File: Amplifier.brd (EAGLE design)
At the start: 60.3 x 55.2 mm, 34 parts, among them IC1 OP213, J1 ARDUINO_R3_SHIELD

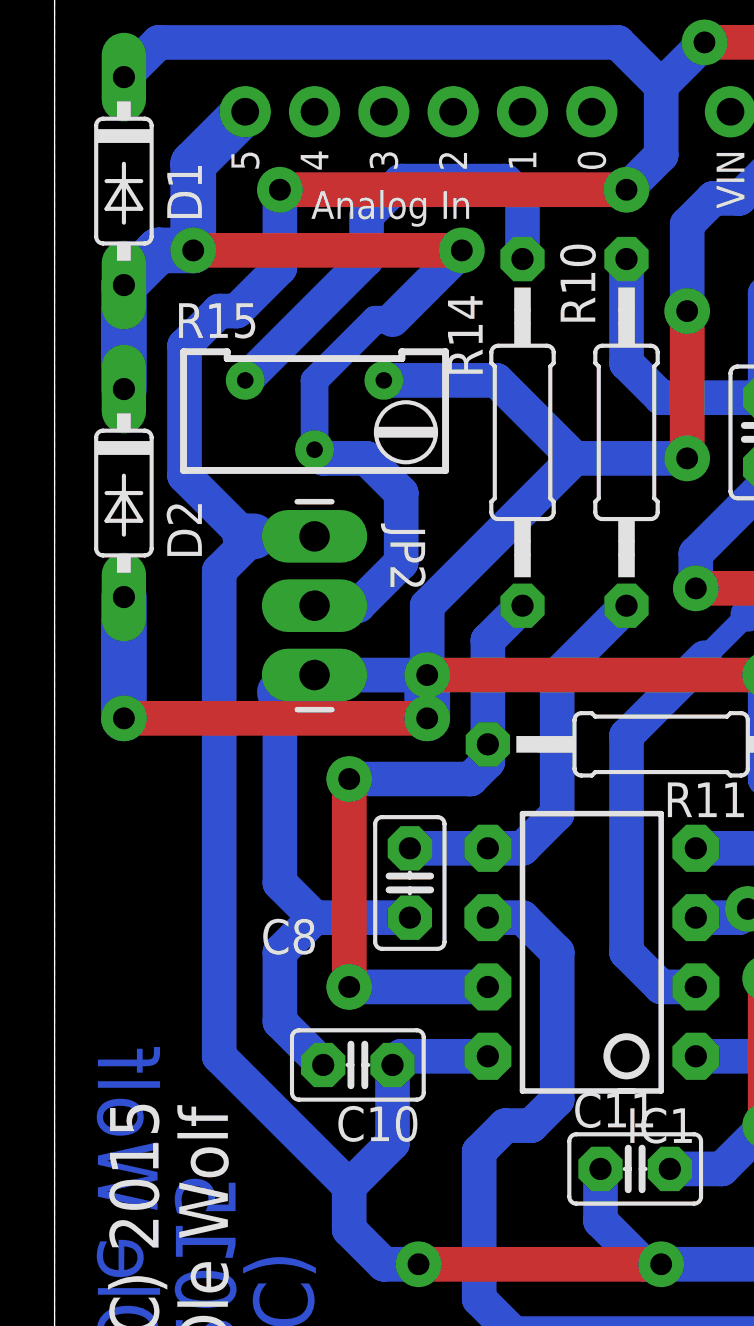
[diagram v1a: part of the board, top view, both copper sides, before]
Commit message: Bug in output stage fixed, redundant capacitor removed.
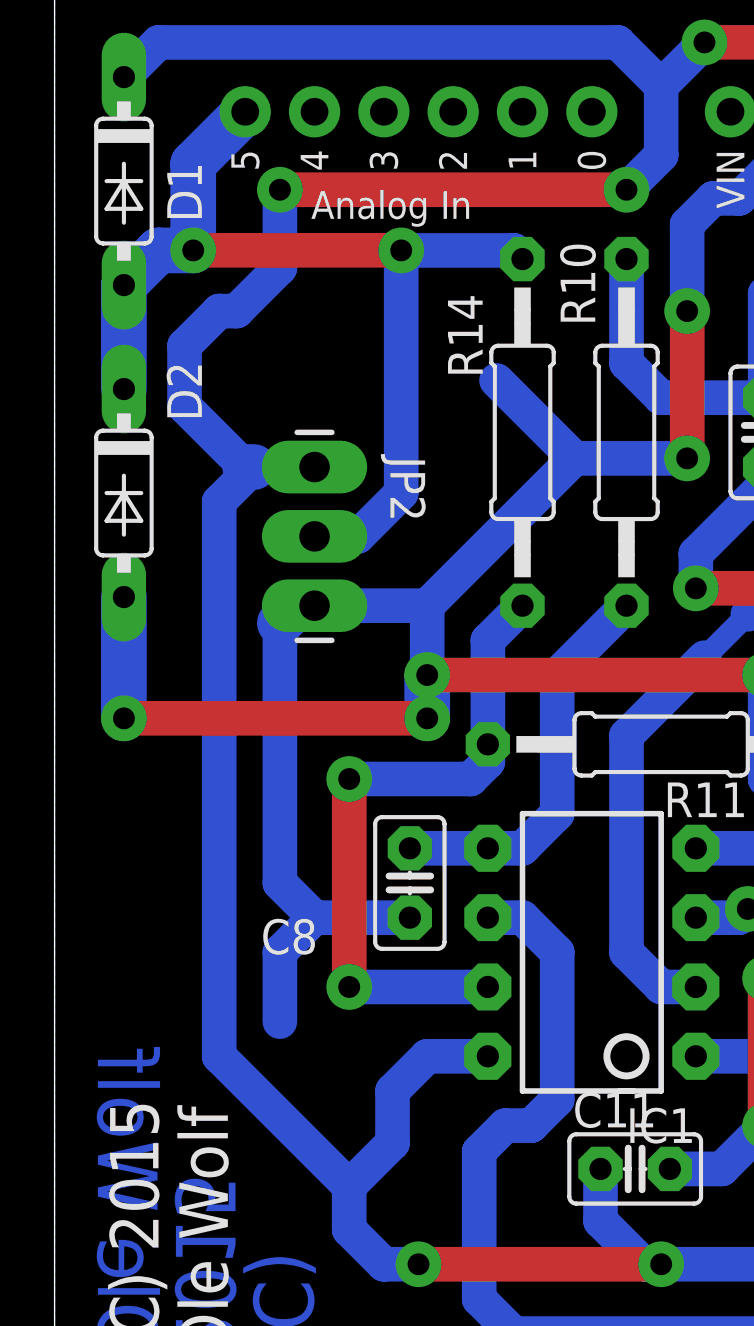
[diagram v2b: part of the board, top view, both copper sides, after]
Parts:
- removed C10: 100n, rcl:C025-025X050
- removed R15: 4k7, rcl:RTRIM64Y
- moved JP2 2.54 mm to (9.53, 32.7)
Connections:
- removed net N$18: R14.1, R15.3
- net GEOPHONE_OUT: now also R14.1; no longer R15.2
- net GND: no longer C10.2, R15.1
- net VCC: no longer C10.1
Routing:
- net N$18: track 16.6 -> 0.00 mm
- net GEOPHONE_OUT: track 42.7 -> 37.7 mm
- net GND: track 166.8 -> 163.0 mm
- net VCC: track 166.8 -> 166.3 mm
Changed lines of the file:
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@@
 <attribute name="VALUE" x="16.4592" y="41.3385" size="1.27" layer="27" ratio="10" rot="R270"/>
 </element>
-<element name="JP2" library="SparkFun-Connectors" package="1X03_LONGPADS" value="Out" x="9.525" y="30.1625" smashed="yes" rot="R90">
-<attribute name="NAME" x="12.3063" y="35.6362" size="1.27" layer="25" ratio="10" rot="SR270"/>
-<attribute name="VALUE" x="5.3975" y="33.02" size="1.27" layer="27" rot="SR270"/>
-</element>
-<element name="C10" library="rcl" package="C025-025X050" value="100n" x="11.1125" y="15.875" smashed="yes" rot="R180">
-<attribute name="NAME" x="13.3985" y="14.351" size="1.27" layer="25" ratio="10" rot="R180"/>
-<attribute name="VALUE" x="13.716" y="12.6365" size="1.27" layer="27" ratio="10" rot="R180"/>
-</element>
-<element name="R15" library="rcl" package="RTRIM64Y" value="4k7" x="9.525" y="40.9575" smashed="yes" rot="R90">
-<attribute name="NAME" x="7.49" y="43.785" size="1.27" layer="25" rot="R180"/>
-<attribute name="VALUE" x="11.6175" y="43.7075" size="1.27" layer="27" rot="R180"/>
+<element name="JP2" library="SparkFun-Connectors" package="1X03_LONGPADS" value="Out" x="9.525" y="32.7025" smashed="yes" rot="R90">
+<attribute name="NAME" x="12.3063" y="38.1762" size="1.27" layer="25" ratio="10" rot="SR270"/>
+<attribute name="VALUE" x="5.3975" y="36.83" size="1.27" layer="27" rot="SR270"/>
 </element>
 <element name="J1" library="SparkFun-Boards" package="UNO_R3_SHIELD" value="ARDUINO_R3_SHIELD" x="61.595" y="0" rot="R90"/>
@@
 </element>
 <element name="D2" library="diode" package="DO35-7" value="1N4148DO35-7" x="2.54" y="36.83" smashed="yes" rot="R270">
-<attribute name="NAME" x="4.1275" y="36.576" size="1.27" layer="25" ratio="10" rot="R270"/>
+<attribute name="NAME" x="4.1275" y="41.656" size="1.27" layer="25" ratio="10" rot="R270"/>
 </element>
 <element name="JP3" library="pinhead" package="1X03" value="" x="48.895" y="50.165" smashed="yes">
@@
 <contactref element="IC1" pad="8"/>
 <contactref element="JP2" pad="3"/>
-<contactref element="C10" pad="1"/>
-<wire x1="7.3025" y1="35.2425" x2="6.0325" y2="33.9725" width="1.27" layer="16"/>
-<wire x1="6.0325" y1="33.9725" x2="6.0325" y2="16.1925" width="1.27" layer="16"/>
-<wire x1="15.875" y1="16.1925" x2="12.7" y2="16.1925" width="1.27" layer="16"/>
-<wire x1="12.7" y1="16.1925" x2="12.3825" y2="15.875" width="1.27" layer="16"/>
+<wire x1="7.3025" y1="37.7825" x2="6.0325" y2="36.5125" width="1.27" layer="16"/>
+<wire x1="6.0325" y1="36.5125" x2="6.0325" y2="16.1925" width="1.27" layer="16"/>
 <wire x1="40.005" y1="6.0325" x2="40.005" y2="7.3025" width="1.27" layer="16"/>
 <wire x1="40.005" y1="7.3025" x2="38.735" y2="8.5725" width="1.27" layer="16"/>
@@
 <wire x1="22.225" y1="8.5725" x2="13.335" y2="8.5725" width="1.27" layer="1"/>
 <via x="13.335" y="8.5725" extent="1-16" drill="0.8" diameter="1.6764" shape="square"/>
-<wire x1="7.3025" y1="35.2425" x2="6.985" y2="35.2425" width="1.6764" layer="16"/>
-<wire x1="6.985" y1="35.2425" x2="4.7625" y2="37.465" width="1.27" layer="16"/>
-<wire x1="4.7625" y1="37.465" x2="4.7625" y2="42.2275" width="1.27" layer="16"/>
+<wire x1="7.3025" y1="37.7825" x2="6.985" y2="37.7825" width="1.6764" layer="16"/>
+<wire x1="6.985" y1="37.7825" x2="4.7625" y2="40.005" width="1.27" layer="16"/>
+<wire x1="4.7625" y1="40.005" x2="4.7625" y2="42.2275" width="1.27" layer="16"/>
 <wire x1="4.7625" y1="42.2275" x2="6.0325" y2="43.4975" width="1.27" layer="16"/>
 <wire x1="6.0325" y1="43.4975" x2="6.6675" y2="43.4975" width="1.27" layer="16"/>
@@
 <wire x1="8.255" y1="45.085" x2="8.255" y2="47.9425" width="1.27" layer="16"/>
 <via x="8.255" y="47.9425" extent="1-16" drill="0.8" diameter="1.6764" shape="square"/>
-<wire x1="9.525" y1="35.2425" x2="7.3025" y2="35.2425" width="1.27" layer="16"/>
+<wire x1="9.525" y1="37.7825" x2="7.3025" y2="37.7825" width="1.27" layer="16"/>
 <wire x1="8.255" y1="47.9425" x2="20.955" y2="47.9425" width="1.27" layer="1"/>
 <via x="20.955" y="47.9425" extent="1-16" drill="0.8" diameter="1.6764" shape="square"/>
@@
 <wire x1="10.795" y1="9.8425" x2="12.065" y2="8.5725" width="1.27" layer="16"/>
 <wire x1="12.065" y1="8.5725" x2="13.335" y2="8.5725" width="1.27" layer="16"/>
-<wire x1="12.3825" y1="15.875" x2="12.3825" y2="13.0175" width="1.27" layer="16"/>
 <wire x1="12.3825" y1="13.0175" x2="10.795" y2="11.43" width="1.27" layer="16"/>
 <contactref element="C11" pad="1"/>
@@
 <wire x1="53.6575" y1="50.8" x2="54.9275" y2="49.53" width="1.27" layer="16"/>
 <wire x1="54.9275" y1="49.53" x2="56.515" y2="49.53" width="1.27" layer="16"/>
+<wire x1="12.3825" y1="13.0175" x2="12.3825" y2="14.9225" width="1.27" layer="16"/>
+<wire x1="15.875" y1="16.1925" x2="13.6525" y2="16.1925" width="1.27" layer="16"/>
+<wire x1="13.6525" y1="16.1925" x2="12.3825" y2="14.9225" width="1.27" layer="16"/>
 </signal>
 <signal name="N$4">
@@
 <contactref element="C8" pad="2"/>
 <contactref element="JP2" pad="1"/>
-<contactref element="C10" pad="2"/>
-<wire x1="8.255" y1="22.5425" x2="8.255" y2="29.5275" width="1.27" layer="16"/>
-<wire x1="8.255" y1="29.5275" x2="8.89" y2="30.1625" width="1.6764" layer="16"/>
-<wire x1="8.89" y1="30.1625" x2="9.525" y2="30.1625" width="1.6764" layer="16"/>
+<wire x1="8.255" y1="22.5425" x2="8.255" y2="32.0675" width="1.27" layer="16"/>
+<wire x1="8.255" y1="32.0675" x2="8.89" y2="32.7025" width="1.6764" layer="16"/>
+<wire x1="8.89" y1="32.7025" x2="9.525" y2="32.7025" width="1.6764" layer="16"/>
 <wire x1="9.525" y1="21.2725" x2="8.255" y2="22.5425" width="1.27" layer="16"/>
-<wire x1="9.8425" y1="15.875" x2="8.255" y2="17.4625" width="1.27" layer="16"/>
 <wire x1="8.255" y1="17.4625" x2="8.255" y2="20.0025" width="1.27" layer="16"/>
 <contactref element="C9" pad="-"/>
@@
 <wire x1="8.255" y1="20.0025" x2="9.525" y2="21.2725" width="1.27" layer="16"/>
 <wire x1="45.085" y1="26.3525" x2="45.085" y2="28.8925" width="1.27" layer="16"/>
-<wire x1="9.525" y1="30.1625" x2="13.6525" y2="30.1625" width="1.27" layer="16"/>
 <wire x1="13.6525" y1="32.7025" x2="13.6525" y2="30.1625" width="1.27" layer="16"/>
 <wire x1="13.6525" y1="32.7025" x2="19.05" y2="38.1" width="1.27" layer="16"/>
@@
 <wire x1="27.94" y1="20.955" x2="27.94" y2="22.5425" width="1.27" layer="16"/>
 <wire x1="27.94" y1="22.5425" x2="26.67" y2="23.8125" width="1.27" layer="16"/>
-<contactref element="R15" pad="1"/>
-<wire x1="12.065" y1="40.9575" x2="16.1925" y2="40.9575" width="1.27" layer="16"/>
 <wire x1="16.1925" y1="40.9575" x2="19.05" y2="38.1" width="1.27" layer="16"/>
+<wire x1="9.525" y1="32.7025" x2="13.6525" y2="32.7025" width="1.27" layer="16"/>
 </signal>
 <signal name="GEOPHONE_OUT">
 <contactref element="JP2" pad="2"/>
 <contactref element="J1" pad="A5"/>
-<wire x1="12.3825" y1="43.18" x2="14.9225" y2="45.72" width="1.27" layer="16"/>
-<via x="14.9225" y="45.72" extent="1-16" drill="0.8" diameter="1.6764" shape="square"/>
-<wire x1="14.9225" y1="45.72" x2="5.08" y2="45.72" width="1.27" layer="1"/>
+<via x="12.7" y="45.72" extent="1-16" drill="0.8" diameter="1.6764" shape="square"/>
+<wire x1="12.7" y1="45.72" x2="5.08" y2="45.72" width="1.27" layer="1"/>
 <via x="5.08" y="45.72" extent="1-16" drill="0.8" diameter="1.6764" shape="square"/>
 <wire x1="5.08" y1="45.72" x2="5.08" y2="48.895" width="1.6764" layer="16"/>
@@
 <wire x1="3.81" y1="45.72" x2="2.54" y2="44.45" width="1.6764" layer="16"/>
 <wire x1="2.54" y1="44.45" x2="2.54" y2="40.64" width="1.6764" layer="16"/>
-<contactref element="R15" pad="2"/>
-<wire x1="9.525" y1="38.4175" x2="9.525" y2="40.9575" width="1.016" layer="16"/>
-<wire x1="9.525" y1="40.9575" x2="11.7475" y2="43.18" width="1.016" layer="16"/>
-<wire x1="11.7475" y1="43.18" x2="12.3825" y2="43.18" width="1.016" layer="16"/>
-<wire x1="9.525" y1="32.7025" x2="11.1125" y2="32.7025" width="1.27" layer="16"/>
-<wire x1="11.1125" y1="32.7025" x2="12.7" y2="34.29" width="1.27" layer="16"/>
-<wire x1="12.7" y1="34.29" x2="12.7" y2="36.83" width="1.27" layer="16"/>
-<wire x1="12.7" y1="36.83" x2="11.43" y2="38.1" width="1.27" layer="16"/>
-<wire x1="11.43" y1="38.1" x2="9.8425" y2="38.1" width="1.27" layer="16"/>
-<wire x1="9.8425" y1="38.1" x2="9.525" y2="38.4175" width="1.27" layer="16"/>
+<wire x1="9.525" y1="35.2425" x2="11.1125" y2="35.2425" width="1.27" layer="16"/>
+<wire x1="11.1125" y1="35.2425" x2="12.7" y2="36.83" width="1.27" layer="16"/>
+<contactref element="R14" pad="1"/>
+<wire x1="12.7" y1="36.83" x2="12.7" y2="45.72" width="1.27" layer="16"/>
+<wire x1="12.7" y1="45.72" x2="16.8275" y2="45.72" width="1.27" layer="16"/>
+<wire x1="16.8275" y1="45.72" x2="17.145" y2="45.4025" width="1.27" layer="16"/>
 </signal>
 <signal name="N$14">
@@
 <wire x1="50.4825" y1="46.99" x2="56.515" y2="46.99" width="1.4224" layer="16"/>
 </signal>
-<signal name="N$18">
-<contactref element="R14" pad="1"/>
-<contactref element="R15" pad="3"/>
-<wire x1="17.145" y1="45.4025" x2="17.145" y2="47.625" width="1.27" layer="16"/>
-<wire x1="17.145" y1="47.625" x2="16.51" y2="48.26" width="1.27" layer="16"/>
-<wire x1="16.51" y1="48.26" x2="12.7" y2="48.26" width="1.27" layer="16"/>
-<wire x1="12.7" y1="48.26" x2="11.43" y2="46.99" width="1.27" layer="16"/>
-<wire x1="11.43" y1="46.99" x2="11.43" y2="45.4025" width="1.27" layer="16"/>
-<wire x1="11.43" y1="45.4025" x2="6.985" y2="40.9575" width="1.27" layer="16"/>
-</signal>
 </signals>
